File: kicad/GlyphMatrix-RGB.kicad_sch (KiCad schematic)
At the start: 76 parts

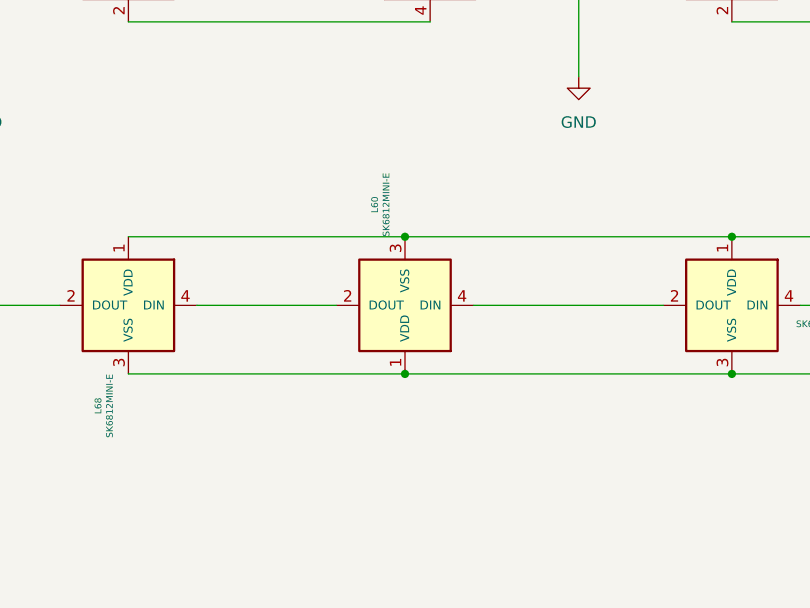
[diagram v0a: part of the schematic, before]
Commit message: fixed LED for GlyphMatrix
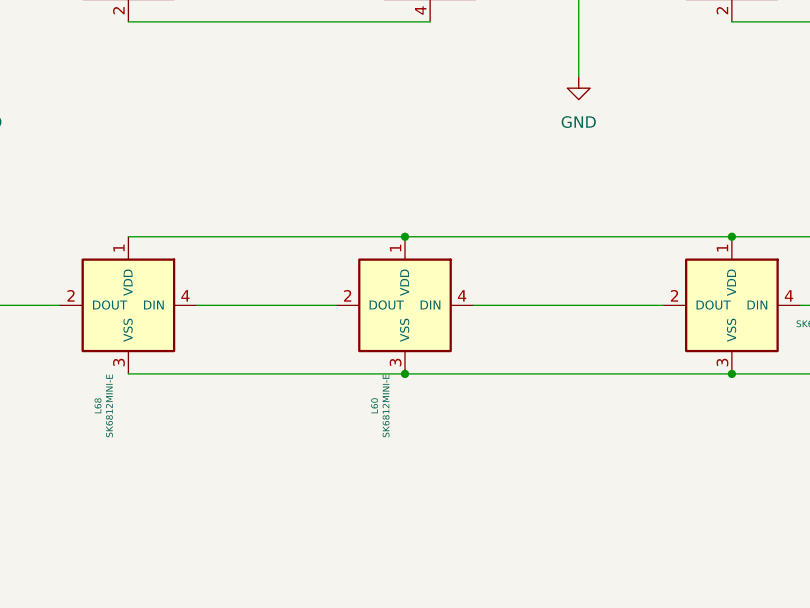
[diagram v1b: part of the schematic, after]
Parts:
- JP1, JP2: footprint TB2086_MISC:SolderJumper-2_P1.3mm_Open_TrianglePad1.0x1.5mm -> Jumper:SolderJumper-2_P1.3mm_Bridged_RoundedPad1.0x1.5mm
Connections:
- net +5V: now also L60.1 (VDD); no longer L60.3 (VSS)
- net GND: now also L60.3 (VSS); no longer L60.1 (VDD)
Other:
- moved on the sheet: L60
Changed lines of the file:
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@@
 			)
 		)
-		(property "Footprint" "TB2086_MISC:SolderJumper-2_P1.3mm_Open_TrianglePad1.0x1.5mm"
+		(property "Footprint" "Jumper:SolderJumper-2_P1.3mm_Bridged_RoundedPad1.0x1.5mm"
 			(at 50.546 196.342 0)
 			(effects
@@
 	(symbol
 		(lib_id "TB2086_LED:SK6812MINI-E")
-		(at 110.744 268.732 180)
+		(at 110.744 268.732 0)
+		(mirror y)
 		(unit 1)
 		(exclude_from_sim no)
@@
 		(dnp no)
 		(property "Reference" "L60"
-			(at 107.3959 257.556 90)
+			(at 107.3959 279.908 90)
 			(effects
 				(font
@@
 		)
 		(property "Value" "SK6812MINI-E"
-			(at 108.6659 257.556 90)
+			(at 108.6659 279.908 90)
 			(effects
 				(font
@@
 		)
 		(property "Footprint" "TB2086_LED_G:LED_SK6812MINI-E"
-			(at 108.204 262.382 0)
+			(at 108.204 275.082 0)
 			(effects
 				(font
@@
 		)
 		(property "Datasheet" ""
-			(at 108.204 262.382 0)
+			(at 108.204 275.082 0)
 			(effects
 				(font
@@
 		)
 		(property "LCSC" "C5149201"
-			(at 107.3959 257.556 0)
+			(at 107.3959 279.908 0)
 			(effects
 				(font
@@
 			)
 		)
-		(property "Footprint" "TB2086_MISC:SolderJumper-2_P1.3mm_Open_TrianglePad1.0x1.5mm"
+		(property "Footprint" "Jumper:SolderJumper-2_P1.3mm_Bridged_RoundedPad1.0x1.5mm"
 			(at 547.116 193.04 0)
 			(effects
